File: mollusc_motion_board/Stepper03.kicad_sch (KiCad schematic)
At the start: 7 parts, among them J3 RJ45 x4, U6 74HC14, U6 SN74AHCT125N

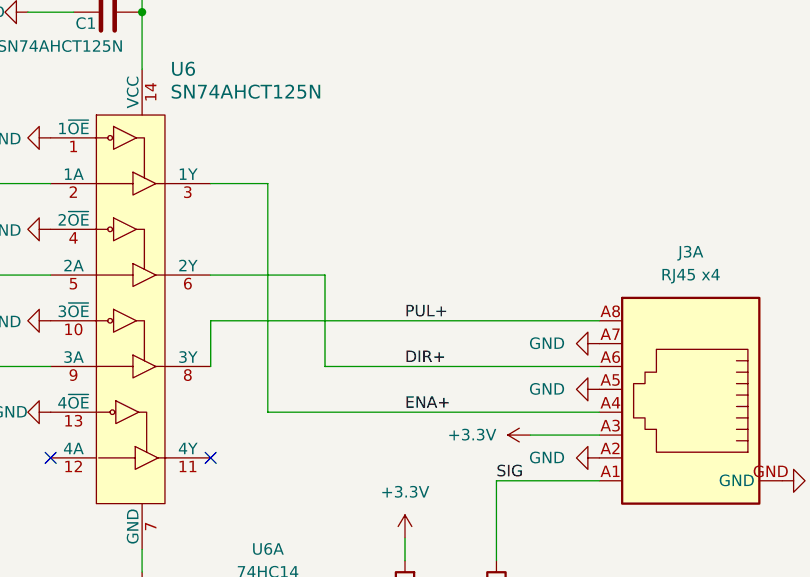
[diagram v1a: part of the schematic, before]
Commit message: adding ethernet jack
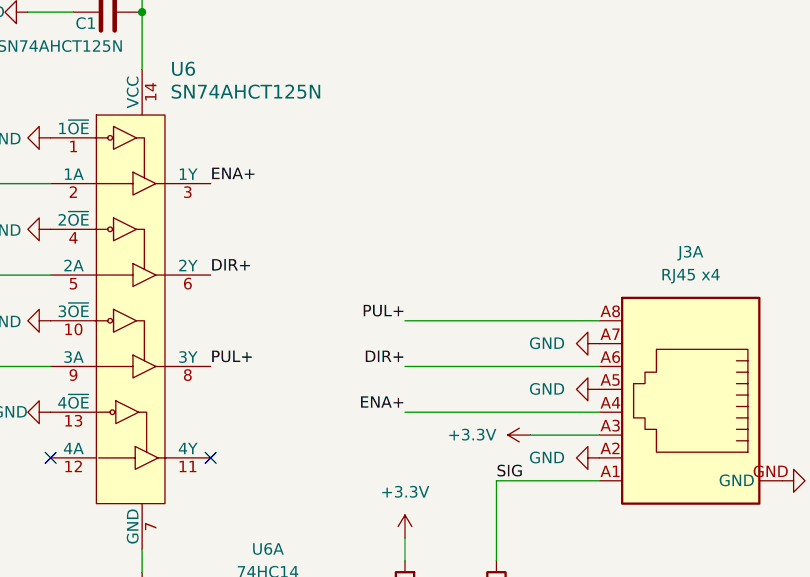
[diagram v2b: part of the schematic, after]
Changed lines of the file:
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@@
   (no_connect (at 127 127))
   (no_connect (at 109.22 127))
-  (wire (pts (xy 139.7 106.68) (xy 139.7 116.84))
-    (stroke (width 0) (type default))
-  )
   (wire (pts (xy 99.06 116.84) (xy 109.22 116.84))
     (stroke (width 0) (type default))
@@
     (stroke (width 0) (type default))
   )
-  (wire (pts (xy 133.35 96.52) (xy 127 96.52))
+  (wire (pts (xy 148.59 111.76) (xy 170.18 111.76))
     (stroke (width 0) (type default))
   )
@@
   )
   (wire (pts (xy 125.73 146.05) (xy 109.22 146.05))
+    (stroke (width 0) (type default))
+  )
+  (wire (pts (xy 148.59 121.92) (xy 170.18 121.92))
     (stroke (width 0) (type default))
   )
@@
     (stroke (width 0) (type default))
   )
-  (wire (pts (xy 133.35 121.92) (xy 133.35 96.52))
-    (stroke (width 0) (type default))
-  )
-  (wire (pts (xy 139.7 116.84) (xy 170.18 116.84))
-    (stroke (width 0) (type default))
-  )
-  (wire (pts (xy 127 111.76) (xy 170.18 111.76))
-    (stroke (width 0) (type default))
-  )
-  (wire (pts (xy 127 111.76) (xy 127 116.84))
-    (stroke (width 0) (type default))
-  )
-  (wire (pts (xy 127 106.68) (xy 139.7 106.68))
-    (stroke (width 0) (type default))
-  )
   (wire (pts (xy 148.59 154.94) (xy 148.59 153.67))
     (stroke (width 0) (type default))
@@
     (stroke (width 0) (type default))
   )
-  (wire (pts (xy 133.35 121.92) (xy 170.18 121.92))
+  (wire (pts (xy 148.59 116.84) (xy 170.18 116.84))
     (stroke (width 0) (type default))
   )
@@
     (effects (font (size 1.27 1.27)) (justify left bottom))
   )
-  (label "ENA+" (at 148.59 121.92 0) (fields_autoplaced)
+  (label "ENA+" (at 148.59 121.92 180) (fields_autoplaced)
+    (effects (font (size 1.27 1.27)) (justify right bottom))
+  )
+  (label "ENA+" (at 127 96.52 0) (fields_autoplaced)
     (effects (font (size 1.27 1.27)) (justify left bottom))
   )
-  (label "DIR+" (at 148.59 116.84 0) (fields_autoplaced)
+  (label "PUL+" (at 127 116.84 0) (fields_autoplaced)
     (effects (font (size 1.27 1.27)) (justify left bottom))
   )
-  (label "PUL+" (at 148.59 111.76 0) (fields_autoplaced)
+  (label "DIR+" (at 148.59 116.84 180) (fields_autoplaced)
+    (effects (font (size 1.27 1.27)) (justify right bottom))
+  )
+  (label "DIR+" (at 127 106.68 0) (fields_autoplaced)
     (effects (font (size 1.27 1.27)) (justify left bottom))
   )
+  (label "PUL+" (at 148.59 111.76 180) (fields_autoplaced)
+    (effects (font (size 1.27 1.27)) (justify right bottom))
+  )
   (hierarchical_label "Stepper_END" (shape output) (at 109.22 146.05 180) (fields_autoplaced)

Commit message: Board v2 wip
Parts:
- C1, C3: value 0.1uF 16V -> 0.1uF 50V; footprint HangOn_Mainboard:R0603 -> molluscmotion:C0603
- R1, R2: footprint HangOn_Mainboard:R0603 -> molluscmotion:R0603
- U6: footprint HangOn_Mainboard:SOIC-14_L8.7-W3.9-P1.27-LS6.0-BL -> molluscmotion:SOIC-14_L8.7-W3.9-P1.27-LS6.0-BL
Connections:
- net GND: no longer J3.GND
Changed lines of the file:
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@@
-    )
-  )
-  (symbol (lib_id "power:GND") (at 190.5 129.54 90) (unit 1)
-    (in_bom yes) (on_board yes) (dnp no)
-    (property "Reference" "#PWR013" (at 196.85 129.54 0)
-      (effects (font (size 1.27 1.27)) hide)
-    )
-    (property "Value" "GND" (at 194.31 129.54 90)
-      (effects (font (size 1.27 1.27)) (justify right))
-    )
-    (property "Footprint" "" (at 190.5 129.54 0)
-      (effects (font (size 1.27 1.27)) hide)
-    )
-    (property "Datasheet" "" (at 190.5 129.54 0)
-      (effects (font (size 1.27 1.27)) hide)
-    )
-    (pin "1")
-    (instances
-      (project "mollusc_motion_board"
-        (path "/351cebb8-982f-46d7-8218-395788e5ce03"
-          (reference "#PWR013") (unit 1)
-        )
-        (path "/351cebb8-982f-46d7-8218-395788e5ce03/679b5948-2929-4082-9ec3-0ebae5348a76"
-          (reference "#PWR013") (unit 1)
-        )
-        (path "/351cebb8-982f-46d7-8218-395788e5ce03/241b4bb9-da37-4994-92a5-1bace8e7dd51"
-          (reference "#PWR013") (unit 1)
-        )
-      )
-      (project "MechanicalTheatre"
-        (path "/7716aab8-fa4d-4c39-bbbe-a68aa4fb9c54/00000000-0000-0000-0000-00006111fd42"
-          (reference "#PWR0153") (unit 1)
-        )
-      )
     )
   )
@@
       (effects (font (size 1.27 1.27)) (justify left))
     )
-    (property "Value" "0.1uF 16V " (at 118.11 73.66 90)
+    (property "Value" "0.1uF 50V " (at 118.11 73.66 90)
       (effects (font (size 1.27 1.27)) (justify left))
     )
-    (property "Footprint" "HangOn_Mainboard:R0603" (at 119.38 76.5048 0)
+    (property "Footprint" "molluscmotion:C0603" (at 119.38 76.5048 0)
       (effects (font (size 1.27 1.27)) hide)
     )
@@
       (effects (font (size 1.27 1.27)) (justify right))
     )
-    (property "Footprint" "HangOn_Mainboard:R0603" (at 150.368 142.24 90)
+    (property "Footprint" "molluscmotion:R0603" (at 150.368 142.24 90)
       (effects (font (size 1.27 1.27)) hide)
     )
@@
       (effects (font (size 1.27 1.27)) (justify left))
     )
-    (property "Value" "0.1uF 16V" (at 151.511 151.003 0)
+    (property "Value" "0.1uF 50V " (at 151.511 151.003 0)
       (effects (font (size 1.27 1.27)) (justify left))
     )
-    (property "Footprint" "HangOn_Mainboard:R0603" (at 149.5552 153.67 0)
+    (property "Footprint" "molluscmotion:C0603" (at 149.5552 153.67 0)
       (effects (font (size 1.27 1.27)) hide)
     )
@@
         )
         (path "/351cebb8-982f-46d7-8218-395788e5ce03/241b4bb9-da37-4994-92a5-1bace8e7dd51"
-          (reference "J4") (unit 1)
+          (reference "J4") (unit 2)
         )
       )
@@
       (effects (font (size 1.524 1.524)) (justify left))
     )
-    (property "Footprint" "HangOn_Mainboard:SOIC-14_L8.7-W3.9-P1.27-LS6.0-BL" (at 124.46 96.52 0)
+    (property "Footprint" "molluscmotion:SOIC-14_L8.7-W3.9-P1.27-LS6.0-BL" (at 124.46 96.52 0)
       (effects (font (size 1.524 1.524)) (justify left) hide)
     )
@@
       (effects (font (size 1.27 1.27)))
     )
-    (property "Footprint" "HangOn_Mainboard:SOIC-14_L8.7-W3.9-P1.27-LS6.0-BL" (at 133.35 146.05 0)
+    (property "Footprint" "molluscmotion:SOIC-14_L8.7-W3.9-P1.27-LS6.0-BL" (at 133.35 146.05 0)
       (effects (font (size 1.27 1.27)) hide)
     )
@@
       (effects (font (size 1.27 1.27)) (justify left))
     )
-    (property "Footprint" "HangOn_Mainboard:R0603" (at 156.972 142.24 90)
-      (effects (font (size 1.27 1.27)) hide)
-    )
+    (property "Footprint" "molluscmotion:R0603" (at 156.972 142.24 90)
+      (effects (font (size 1.27 1.27)) hide)
+    )

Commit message: PCB v1.2 Layout
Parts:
- added D5: ESD5Z5_0T1G, molluscmotion:SOD-523F_L1.2-W0.8-LS1.7-RD, symbol molluscmotion:ESD5Z5_0T1G
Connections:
- net GND: now also D5.2 (A)
- net at C3.1, R1.1, R2.2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: now also D5.1 (C)
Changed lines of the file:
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@@
 (kicad_sch (version 20230121) (generator eeschema)
   (paper "A4")
+  (junction (at 158.75 146.05) (diameter 0) (color 0 0 0 0)
+  )
   (junction (at 148.59 146.05) (diameter 0) (color 0 0 0 0)
   )
   (junction (at 119.38 77.47) (diameter 0) (color 0 0 0 0)
+  )
+  (junction (at 153.67 157.48) (diameter 0) (color 0 0 0 0)
   )
   (no_connect (at 127 127))
   (no_connect (at 109.22 127))
+  (wire (pts (xy 148.59 153.67) (xy 148.59 157.48))
+    (stroke (width 0) (type default))
+  )
   (wire (pts (xy 99.06 116.84) (xy 109.22 116.84))
     (stroke (width 0) (type default))
   )
+  (wire (pts (xy 158.75 156.21) (xy 158.75 157.48))
+    (stroke (width 0) (type default))
+  )
   (wire (pts (xy 148.59 146.05) (xy 158.75 146.05))
     (stroke (width 0) (type default))
@@
     (stroke (width 0) (type default))
   )
+  (wire (pts (xy 153.67 157.48) (xy 158.75 157.48))
+    (stroke (width 0) (type default))
+  )
+  (wire (pts (xy 153.67 157.48) (xy 153.67 160.02))
+    (stroke (width 0) (type default))
+  )
   (wire (pts (xy 148.59 121.92) (xy 170.18 121.92))
     (stroke (width 0) (type default))
@@
     (stroke (width 0) (type default))
   )
-  (wire (pts (xy 148.59 154.94) (xy 148.59 153.67))
+  (wire (pts (xy 148.59 157.48) (xy 153.67 157.48))
     (stroke (width 0) (type default))
   )
@@
         (path "/7716aab8-fa4d-4c39-bbbe-a68aa4fb9c54/00000000-0000-0000-0000-00006111fd42"
           (reference "#PWR049") (unit 1)
+        )
+      )
+    )
+  )
+  (symbol (lib_id "power:GND") (at 153.67 160.02 0) (unit 1)
+    (in_bom yes) (on_board yes) (dnp no)
+    (property "Reference" "#PWR07" (at 153.67 166.37 0)
+      (effects (font (size 1.27 1.27)) hide)
+    )
+    (property "Value" "GND" (at 156.21 163.83 0)
+      (effects (font (size 1.27 1.27)) (justify right))
+    )
+    (property "Footprint" "" (at 153.67 160.02 0)
+      (effects (font (size 1.27 1.27)) hide)
+    )
+    (property "Datasheet" "" (at 153.67 160.02 0)
+      (effects (font (size 1.27 1.27)) hide)
+    )
+    (pin "1")
+    (instances
+      (project "mollusc_motion_board"
+        (path "/351cebb8-982f-46d7-8218-395788e5ce03"
+          (reference "#PWR07") (unit 1)
+        )
+        (path "/351cebb8-982f-46d7-8218-395788e5ce03/679b5948-2929-4082-9ec3-0ebae5348a76"
+          (reference "#PWR07") (unit 1)
+        )
+        (path "/351cebb8-982f-46d7-8218-395788e5ce03/c416ce84-8678-4ab5-ab91-bfcc4d019431"
+          (reference "#PWR013") (unit 1)
+        )
+        (path "/351cebb8-982f-46d7-8218-395788e5ce03/241b4bb9-da37-4994-92a5-1bace8e7dd51"
+          (reference "#PWR020") (unit 1)
+        )
+      )
+      (project "MechanicalTheatre"
+        (path "/7716aab8-fa4d-4c39-bbbe-a68aa4fb9c54/00000000-0000-0000-0000-00006111fd42"
+          (reference "#PWR063") (unit 1)
         )
       )
@@
   (symbol (lib_id "Device:C") (at 148.59 149.86 0) (unit 1)
     (in_bom yes) (on_board yes) (dnp no)
-    (property "Reference" "C3" (at 151.511 148.6916 0)
+    (property "Reference" "C3" (at 143.51 151.13 0)
       (effects (font (size 1.27 1.27)) (justify left))
     )
-    (property "Value" "0.1uF 50V " (at 151.511 151.003 0)
+    (property "Value" "0.1uF 50V " (at 142.24 153.67 0)
       (effects (font (size 1.27 1.27)) (justify left))
     )
@@
     )
   )
-  (symbol (lib_id "power:GND") (at 148.59 154.94 0) (unit 1)
-    (in_bom yes) (on_board yes) (dnp no)
-    (property "Reference" "#PWR07" (at 148.59 161.29 0)
-      (effects (font (size 1.27 1.27)) hide)
-    )
-    (property "Value" "GND" (at 147.32 156.21 0)
-      (effects (font (size 1.27 1.27)) (justify right))
-    )
-    (property "Footprint" "" (at 148.59 154.94 0)
-      (effects (font (size 1.27 1.27)) hide)
-    )
-    (property "Datasheet" "" (at 148.59 154.94 0)
-      (effects (font (size 1.27 1.27)) hide)
-    )
-    (pin "1")
-    (instances
-      (project "mollusc_motion_board"
-        (path "/351cebb8-982f-46d7-8218-395788e5ce03"
-          (reference "#PWR07") (unit 1)
-        )
-        (path "/351cebb8-982f-46d7-8218-395788e5ce03/679b5948-2929-4082-9ec3-0ebae5348a76"
-          (reference "#PWR07") (unit 1)
-        )
-        (path "/351cebb8-982f-46d7-8218-395788e5ce03/241b4bb9-da37-4994-92a5-1bace8e7dd51"
-          (reference "#PWR032") (unit 1)
-        )
-      )
-      (project "MechanicalTheatre"
-        (path "/7716aab8-fa4d-4c39-bbbe-a68aa4fb9c54/00000000-0000-0000-0000-00006111fd42"
-          (reference "#PWR063") (unit 1)
-        )
-      )
-    )
-  )
   (symbol (lib_id "74xx:74HC14") (at 133.35 146.05 180) (unit 1)
     (in_bom yes) (on_board yes) (dnp no) (fields_autoplaced)
@@
         )
       )
+    )
+  )
+  (symbol (lib_id "molluscmotion:ESD5Z5_0T1G") (at 158.75 151.13 270) (unit 1)
+    (in_bom yes) (on_board yes) (dnp no)
+    (property "Reference" "D5" (at 162.56 152.4 90)
+      (effects (font (size 1.27 1.27)))
+    )
+    (property "Value" "ESD5Z5_0T1G" (at 166.37 154.94 90)
+      (effects (font (size 1.27 1.27)))
+    )
+    (property "Footprint" "molluscmotion:SOD-523F_L1.2-W0.8-LS1.7-RD" (at 148.59 151.13 0)
+      (effects (font (size 1.27 1.27) italic) hide)
+    )
+    (property "Datasheet" "https://item.szlcsc.com/235389.html" (at 158.877 148.844 0)
+      (effects (font (size 1.27 1.27)) (justify left) hide)
+    )
+    (property "LCSC" "C82044" (at 158.75 151.13 0)
+      (effects (font (size 1.27 1.27)) hide)
+    )
+    (pin "1")
+    (pin "2")
+    (instances
+      (project "mollusc_motion_board"
+        (path "/351cebb8-982f-46d7-8218-395788e5ce03/679b5948-2929-4082-9ec3-0ebae5348a76"
+          (reference "D5") (unit 1)
+        )
+        (path "/351cebb8-982f-46d7-8218-395788e5ce03/c416ce84-8678-4ab5-ab91-bfcc4d019431"
+          (reference "D4") (unit 1)
+        )
+        (path "/351cebb8-982f-46d7-8218-395788e5ce03/241b4bb9-da37-4994-92a5-1bace8e7dd51"
+          (reference "D6") (unit 1)
+        )
+      )
